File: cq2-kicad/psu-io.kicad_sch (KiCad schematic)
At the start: 44 parts, among them IC1 DAC80502, U24 LM27762, U25 74LVC2G125, U26 74LVC2G125, U27 100 Mb/s, U28 ADS1118, U29 74LVC2G125, U30 74LVC2G125

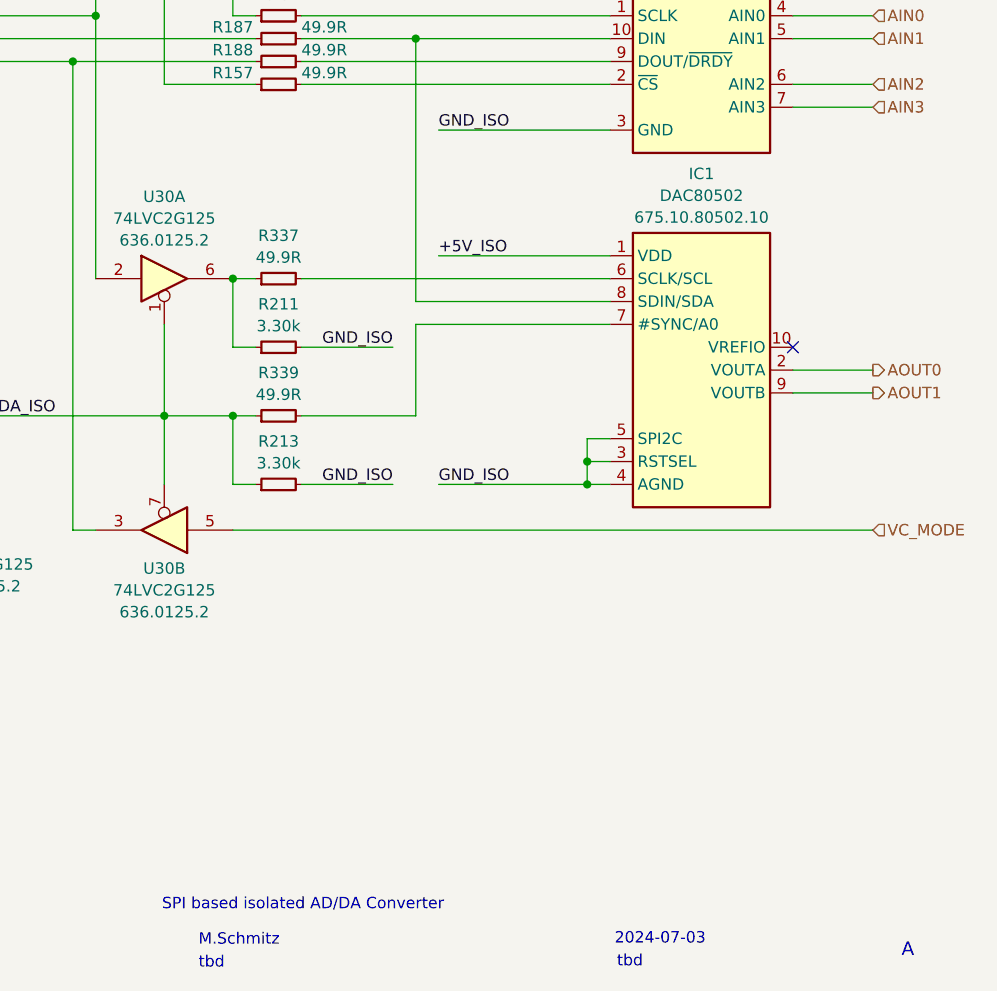
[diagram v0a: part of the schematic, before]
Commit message: drc checked before panalization
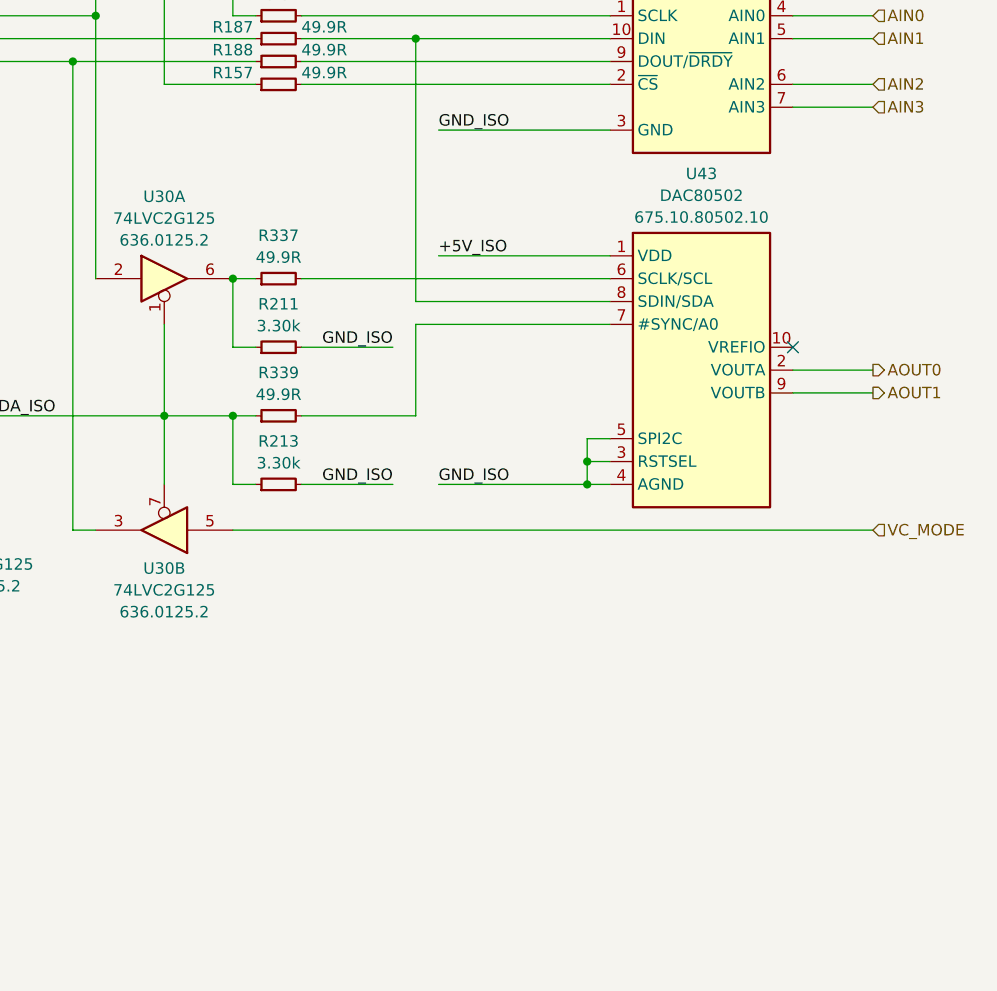
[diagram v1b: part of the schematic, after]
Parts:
- U43: renamed from IC1; Lifecycle review pending CQ2 -> ERP1 pending CQ2; Outline (none) -> SMT WSON10
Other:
- note removed: "2024-07-03"
- note removed: "A"
- note removed: "M.Schmitz"
- note removed: "SPI based isolated AD/DA Converter"
- note removed: "tbd"
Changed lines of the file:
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@@
 	(title_block
 		(title "CQ2")
-		(date "2024-07-17")
+		(date "2024-07-31")
 		(rev "0")
+		(comment 1 "SPI based isolated AD/DA Converter")
+		(comment 2 "Manfred Schmitz")
+		(comment 3 "tbd")
+		(comment 4 "2024-07-03")
+		(comment 5 "tbd")
+		(comment 6 "A")
 	)
 	(junction
@@
 		)
 	)
-	(text "A"
-		(exclude_from_sim no)
-		(at 269.875 192.405 0)
-		(effects
-			(font
-				(size 1.4986 1.4986)
-			)
-			(justify left bottom)
-		)
-	)
-	(text "M.Schmitz"
-		(exclude_from_sim no)
-		(at 191.77 191.135 0)
-		(effects
-			(font
-				(size 1.27 1.27)
-			)
-			(justify left bottom)
-		)
-	)
-	(text "2024-07-03"
-		(exclude_from_sim no)
-		(at 237.998 191.008 0)
-		(effects
-			(font
-				(size 1.27 1.27)
-			)
-			(justify left bottom)
-		)
-	)
-	(text "tbd"
-		(exclude_from_sim no)
-		(at 238.252 193.548 0)
-		(effects
-			(font
-				(size 1.27 1.27)
-			)
-			(justify left bottom)
-		)
-	)
 	(text "-1.2V"
 		(exclude_from_sim no)
@@
 		)
 	)
-	(text "tbd"
-		(exclude_from_sim no)
-		(at 191.77 193.675 0)
-		(effects
-			(font
-				(size 1.27 1.27)
-			)
-			(justify left bottom)
-		)
-	)
-	(text "SPI based isolated AD/DA Converter"
-		(exclude_from_sim no)
-		(at 187.706 187.198 0)
-		(effects
-			(font
-				(size 1.27 1.27)
-			)
-			(justify left bottom)
-		)
-	)
 	(label "+3V3_ISO_D"
 		(at 106.68 140.97 0)
@@
 		(dnp no)
 		(fields_autoplaced yes)
-		(property "Reference" "IC1"
+		(property "Reference" "U43"
 			(at 247.65 105.1913 0)
 			(effects
@@
 			)
 		)
-		(property "Description" "Analog DAC - SMT"
+		(property "Description" "Analog DAC"
 			(at 247.65 127 0)
 			(effects
@@
 			)
 		)
-		(property "Lifecycle" "review pending CQ2"
+		(property "Lifecycle" "ERP1 pending CQ2"
 			(at 247.65 127 0)
 			(effects
@@
 			)
 		)
-		(property "Outline" ""
+		(property "Outline" "SMT WSON10"
 			(at 247.65 127 0)
 			(effects
@@
 			(project "cq2"
 				(path "/b7250307-01ed-4101-9d2a-e447f7e762c6/3fc2b017-f168-44ab-b635-d30322457b0e/1495dad5-83ea-4609-804f-2940cadedc39"
-					(reference "IC1")
+					(reference "U43")
 					(unit 1)
 				)
 				(path "/b7250307-01ed-4101-9d2a-e447f7e762c6/699e04ef-9f87-46ae-839a-2e051ef22e36/1495dad5-83ea-4609-804f-2940cadedc39"
-					(reference "IC2")
+					(reference "U45")
 					(unit 1)
 				)

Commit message: Production documents new
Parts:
- U27: ERP2 670.70.7840.01 -> 670.70.7841.01; MPN TI ISOW7840DWE -> TI ISOW7841DWE
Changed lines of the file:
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@@
 			)
 		)
-		(property "ERP2" "670.70.7840.01"
+		(property "ERP2" "670.70.7841.01"
 			(at 96.52 73.2099 0)
 			(effects
@@
 			)
 		)
-		(property "MPN" "TI ISOW7840DWE"
+		(property "MPN" "TI ISOW7841DWE"
 			(at 96.52 87.63 0)
 			(effects

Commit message: cq2 adapter in work
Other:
- note added: "EN- muss an +3.3V"
- note added: "R205 R209 R290 R294 24 k - Vout = 3.1V"
